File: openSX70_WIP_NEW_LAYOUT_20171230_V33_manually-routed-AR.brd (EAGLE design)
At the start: 95.9 x 27.9 mm, 37 parts, among them Q1 5.8A/30V/35mΩ, Q2 5.8A/30V/35mΩ, U1 ATMEGA328P_TQFP, U3 BH1750FVI-TR, Y1 CSTCE16M0V53-R0

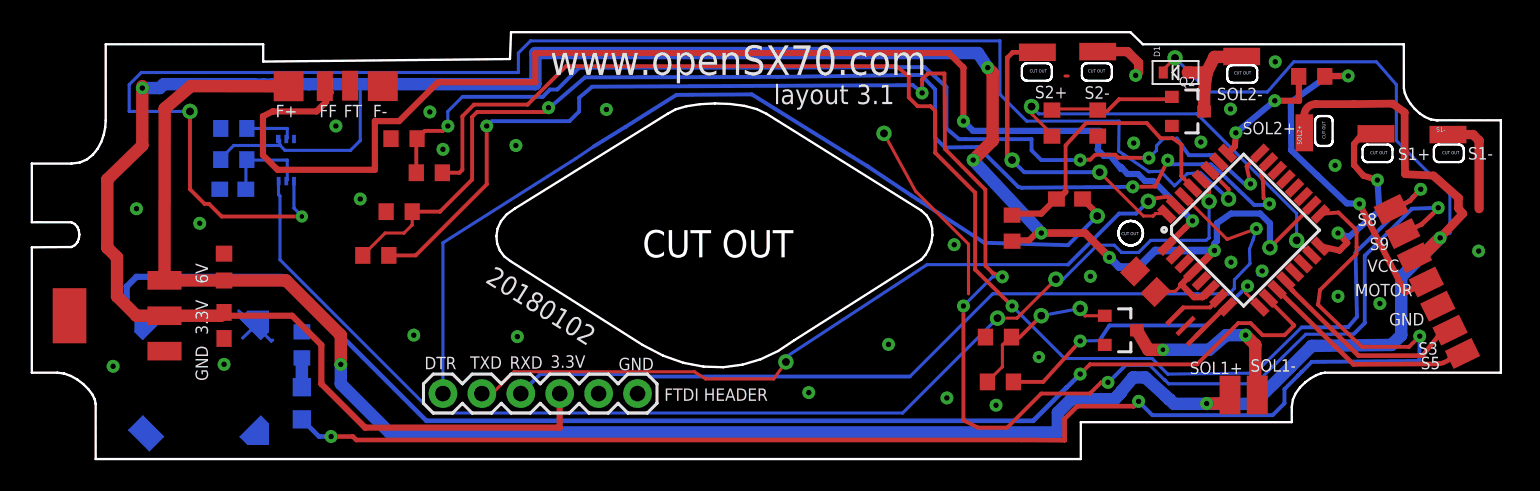
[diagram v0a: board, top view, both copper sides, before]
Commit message: New version 3.3 changed diode to DZ2J033
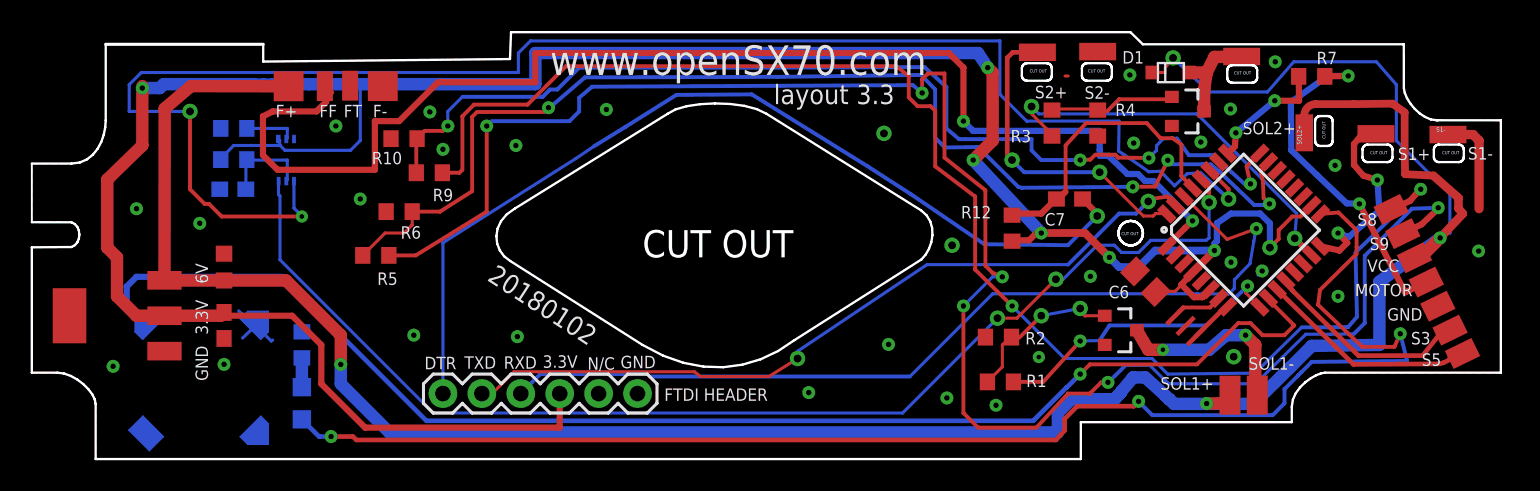
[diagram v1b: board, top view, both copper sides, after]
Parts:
- D1: value (none) -> DZ2J33X0L; device adafruit:SOD-523 -> openSX70:SMINI2
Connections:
- net 6V: now also D1.P$1; no longer D1.K
- net SOL2-: now also D1.P$2; no longer D1.A
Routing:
- net GND: track 27.8 -> 11.8 mm
- net LED: track 96.1 -> 94.1 mm
- net S9@6V: track 114.2 -> 114.9 mm
- net BUZZER: track 90.9 -> 90.2 mm
- net 6V: track 172.7 -> 173.3 mm
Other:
- board text added: "B+"
- board text added: "DUMMY"
- board text added: "LED"
- board text added: "LIGHTMETER"
- board text added: "N/C"
- board text added: "layout 3.3"
- board text removed: "LIGHT METER"
- board text removed: "SOL2-"
- board text removed: "layout 3.1"
